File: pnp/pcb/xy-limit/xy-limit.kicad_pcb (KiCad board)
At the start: 2 copper layers, 98 x 27 mm, 6 parts, among them J1 Conn_01x04_Socket, SW1 X_LIM, SW2 Y_LIM

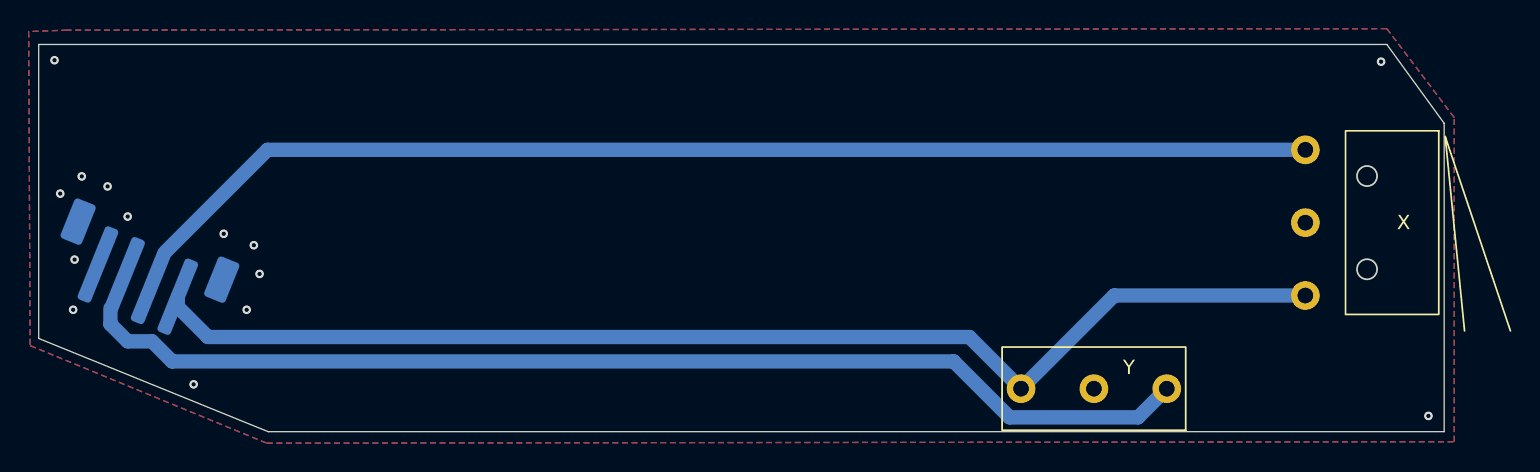
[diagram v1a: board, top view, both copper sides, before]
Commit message: adds new xy limit and rev05b1 mobo to cad
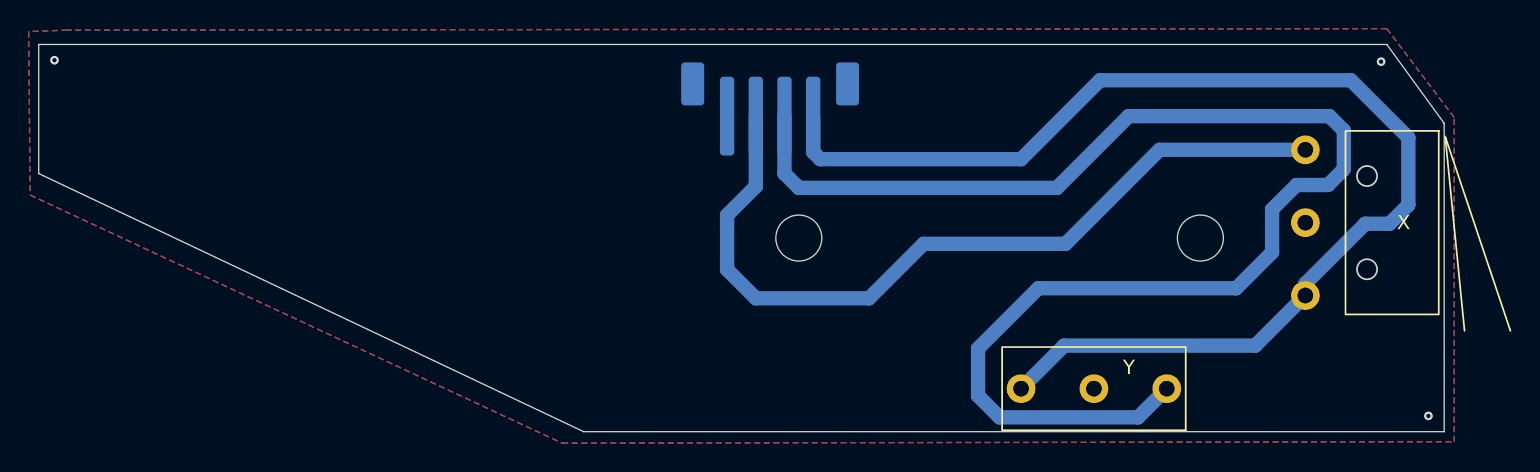
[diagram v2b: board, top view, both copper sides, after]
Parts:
- removed the G*** at (-60.8, -14.1)
- removed J1: Conn_01x04_Socket, Connector_JST:JST_PH_B4B-PH-SM4-TB_1x04-1MP_P2.00mm_Vertical
- added J2: Conn_01x04_MountingPin, Connector_JST:JST_PH_B4B-PH-SM4-TB_1x04-1MP_P2.00mm_Vertical, B.Cu at (-47.0, -22.5)
- moved kibuzzard-65F47CEB 61.5 mm to (-34.0, -23.5)
- moved G*** 60.1 mm to (-75.7, -18.5)
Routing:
- net X_SIG: track 82.5 -> 57.0 mm
- net Y_SIG: track 78.3 -> 98.9 mm
- net +3V3: track 84.4 -> 85.6 mm
- net GND: vias 14 -> 3
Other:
- outline, holes or cut-outs redrawn

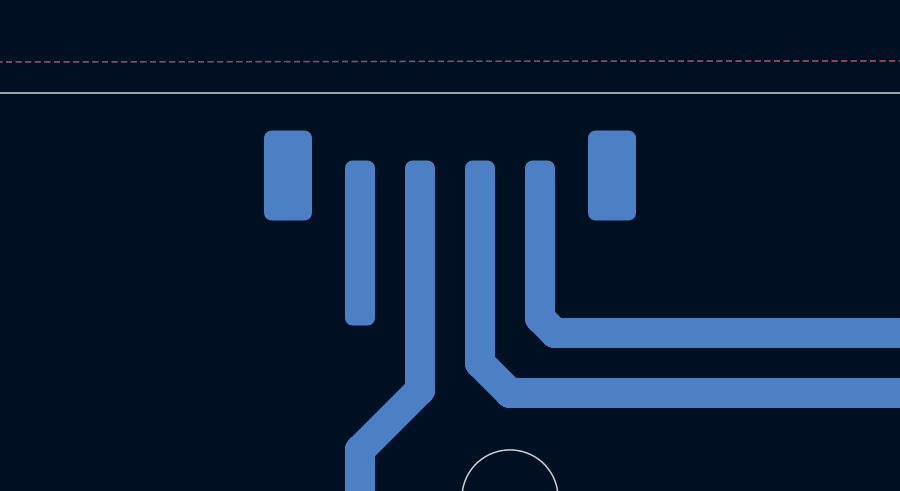
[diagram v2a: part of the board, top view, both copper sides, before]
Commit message: represents REV00b1 of both xy limit and z limit boards
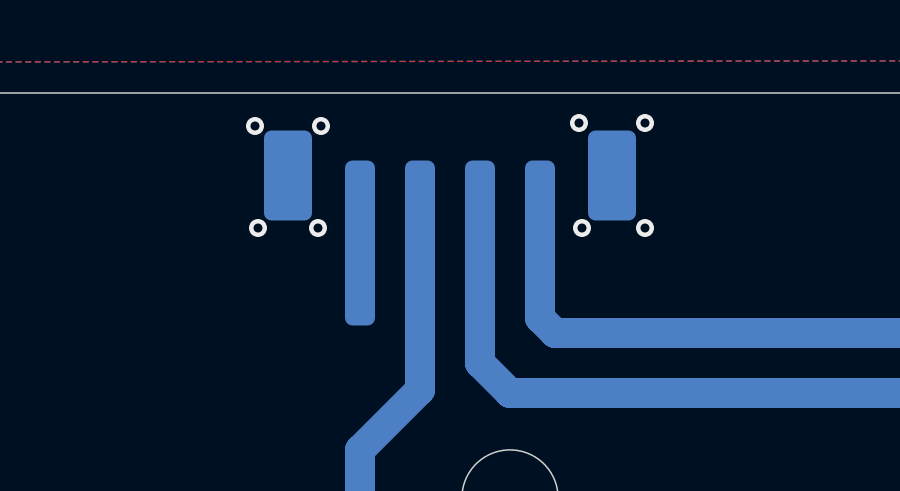
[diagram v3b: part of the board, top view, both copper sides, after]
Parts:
- moved G*** 72.6 mm to (-4.60, -3.80)
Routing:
- net GND: vias 3 -> 11
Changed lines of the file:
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@@
       (drillshape 0)
       (scaleselection 1)
-      (outputdirectory "out/")
+      (outputdirectory "out/REV0B1/")
     )
   )
@@
   )
   (footprint "index:goblin" (layer "B.Cu")
-    (at -75.7 -18.5 180)
+    (at -4.6 -3.8 180)
     (attr through_hole)
     (fp_text reference "G***" (at 0 0) (layer "B.SilkS") hide
@@
   (segment (start -32.5 -5.8) (end -28.3 -10) (width 1) (layer "B.Cu") (net 3))
   (segment (start -7.033225 -18.266775) (end -7 -18.354381) (width 1) (layer "B.Cu") (net 3))
+  (via (at -51.3 -25.9) (size 0.6) (drill 0.3) (layers "F.Cu" "B.Cu") (free) (net 4))
   (via (at -4.4 -25.8) (size 0.6) (drill 0.3) (layers "F.Cu" "B.Cu") (free) (net 4))
+  (via (at -53.5 -25.9) (size 0.6) (drill 0.3) (layers "F.Cu" "B.Cu") (free) (net 4))
+  (via (at -40.5 -22.5) (size 0.6) (drill 0.3) (layers "F.Cu" "B.Cu") (free) (net 4))
   (via (at -1.1 -1.1) (size 0.6) (drill 0.3) (layers "F.Cu" "B.Cu") (free) (net 4))
+  (via (at -42.6 -22.5) (size 0.6) (drill 0.3) (layers "F.Cu" "B.Cu") (free) (net 4))
+  (via (at -40.5 -26) (size 0.6) (drill 0.3) (layers "F.Cu" "B.Cu") (free) (net 4))
+  (via (at -51.4 -22.5) (size 0.6) (drill 0.3) (layers "F.Cu" "B.Cu") (free) (net 4))
+  (via (at -53.4 -22.5) (size 0.6) (drill 0.3) (layers "F.Cu" "B.Cu") (free) (net 4))
+  (via (at -42.7 -26) (size 0.6) (drill 0.3) (layers "F.Cu" "B.Cu") (free) (net 4))
   (via (at -96.9 -25.9) (size 0.6) (drill 0.3) (layers "F.Cu" "B.Cu") (free) (net 4))
+  (zone (net 0) (net_name "") (layer "F.Cu") (hatch edge 0.5)
+    (connect_pads (clearance 0))
+    (min_thickness 0.25) (filled_areas_thickness no)
+    (keepout (tracks not_allowed) (vias not_allowed) (pads not_allowed) (copperpour not_allowed) (footprints allowed))
+    (fill (thermal_gap 0.5) (thermal_bridge_width 0.5))
+    (polygon
+      (pts
+        (xy -41 -13.5)
+        (xy -41.019261 -13.892069)
+        (xy -41.076859 -14.280361)
+        (xy -41.172239 -14.661139)
+        (xy -41.304482 -15.030734)
+        (xy -41.472315 -15.385587)
+        (xy -41.674122 -15.722281)
+        (xy -41.907958 -16.037573)
+        (xy -42.171573 -16.328427)
+        (xy -42.462427 -16.592042)
+        (xy -42.777719 -16.825878)
+        (xy -43.114413 -17.027685)
+        (xy -43.469266 -17.195518)
+        (xy -43.838861 -17.327761)
+        (xy -44.219639 -17.423141)
+        (xy -44.607931 -17.480739)
+        (xy -45 -17.5)
+        (xy -45.392069 -17.480739)
+        (xy -45.780361 -17.423141)
+        (xy -46.161139 -17.327761)
+        (xy -46.530734 -17.195518)
+        (xy -46.885587 -17.027685)
+        (xy -47.222281 -16.825878)
+        (xy -47.537573 -16.592042)
+        (xy -47.828427 -16.328427)
+        (xy -48.092042 -16.037573)
+        (xy -48.325878 -15.722281)
+        (xy -48.527685 -15.385587)
+        (xy -48.695518 -15.030734)
+        (xy -48.827761 -14.661139)
+        (xy -48.923141 -14.280361)
+        (xy -48.980739 -13.892069)
+        (xy -49 -13.5)
+        (xy -48.980739 -13.107931)
+        (xy -48.923141 -12.719639)
+        (xy -48.827761 -12.338861)
+        (xy -48.695518 -11.969266)
+        (xy -48.527685 -11.614413)
+        (xy -48.325878 -11.277719)
+        (xy -48.092042 -10.962427)
+        (xy -47.828427 -10.671573)
+        (xy -47.537573 -10.407958)
+        (xy -47.222281 -10.174122)
+        (xy -46.885587 -9.972315)
+        (xy -46.530734 -9.804482)
+        (xy -46.161139 -9.672239)
+        (xy -45.780361 -9.576859)
+        (xy -45.392069 -9.519261)
+        (xy -45 -9.5)
+        (xy -44.607931 -9.519261)
+        (xy -44.219639 -9.576859)
+        (xy -43.838861 -9.672239)
+        (xy -43.469266 -9.804482)
+        (xy -43.114413 -9.972315)
+        (xy -42.777719 -10.174122)
+        (xy -42.462427 -10.407958)
+        (xy -42.171573 -10.671573)
+        (xy -41.907958 -10.962427)
+        (xy -41.674122 -11.277719)
+        (xy -41.472315 -11.614413)
+        (xy -41.304482 -11.969266)
+        (xy -41.172239 -12.338861)
+        (xy -41.076859 -12.719639)
+        (xy -41.019261 -13.107931)
+      )
+    )
+  )
+  (zone (net 0) (net_name "") (layer "F.Cu") (hatch edge 0.5)
+    (connect_pads (clearance 0))
+    (min_thickness 0.25) (filled_areas_thickness no)
+    (keepout (tracks not_allowed) (vias not_allowed) (pads not_allowed) (copperpour not_allowed) (footprints allowed))
+    (fill (thermal_gap 0.5) (thermal_bridge_width 0.5))
+    (polygon
+      (pts
+        (xy -13 -13.5)
+        (xy -13.019261 -13.892069)
+        (xy -13.076859 -14.280361)
+        (xy -13.172239 -14.661139)
+        (xy -13.304482 -15.030734)
+        (xy -13.472315 -15.385587)
+        (xy -13.674122 -15.722281)
+        (xy -13.907958 -16.037573)
+        (xy -14.171573 -16.328427)
+        (xy -14.462427 -16.592042)
+        (xy -14.777719 -16.825878)
+        (xy -15.114413 -17.027685)
+        (xy -15.469266 -17.195518)
+        (xy -15.838861 -17.327761)
+        (xy -16.219639 -17.423141)
+        (xy -16.607931 -17.480739)
+        (xy -17 -17.5)
+        (xy -17.392069 -17.480739)
+        (xy -17.780361 -17.423141)
+        (xy -18.161139 -17.327761)
+        (xy -18.530734 -17.195518)
+        (xy -18.885587 -17.027685)
+        (xy -19.222281 -16.825878)
+        (xy -19.537573 -16.592042)
+        (xy -19.828427 -16.328427)
+        (xy -20.092042 -16.037573)
+        (xy -20.325878 -15.722281)
+        (xy -20.527685 -15.385587)
+        (xy -20.695518 -15.030734)
+        (xy -20.827761 -14.661139)
+        (xy -20.923141 -14.280361)
+        (xy -20.980739 -13.892069)
+        (xy -21 -13.5)
+        (xy -20.980739 -13.107931)
+        (xy -20.923141 -12.719639)
+        (xy -20.827761 -12.338861)
+        (xy -20.695518 -11.969266)
+        (xy -20.527685 -11.614413)
+        (xy -20.325878 -11.277719)
+        (xy -20.092042 -10.962427)
+        (xy -19.828427 -10.671573)
+        (xy -19.537573 -10.407958)
+        (xy -19.222281 -10.174122)
+        (xy -18.885587 -9.972315)
+        (xy -18.530734 -9.804482)
+        (xy -18.161139 -9.672239)
+        (xy -17.780361 -9.576859)
+        (xy -17.392069 -9.519261)
+        (xy -17 -9.5)
+        (xy -16.607931 -9.519261)
+        (xy -16.219639 -9.576859)
+        (xy -15.838861 -9.672239)
+        (xy -15.469266 -9.804482)
+        (xy -15.114413 -9.972315)
+        (xy -14.777719 -10.174122)
+        (xy -14.462427 -10.407958)
+        (xy -14.171573 -10.671573)
+        (xy -13.907958 -10.962427)
+        (xy -13.674122 -11.277719)
+        (xy -13.472315 -11.614413)
+        (xy -13.304482 -11.969266)
+        (xy -13.172239 -12.338861)
+        (xy -13.076859 -12.719639)
+        (xy -13.019261 -13.107931)
+      )
+    )
+  )
   (zone (net 4) (net_name "GND") (layers "F&B.Cu") (hatch edge 0.5)
     (connect_pads (clearance 0.5))

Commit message: updates with all current v4 pcbs
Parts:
- moved G*** 52.4 mm to (-57.0, -5.00)
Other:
- board text added: "REV00"
